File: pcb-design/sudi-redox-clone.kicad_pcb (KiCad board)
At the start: 2 copper layers, 141.8 x 99.4 mm, 143 parts, among them J1 SIDE_CON, J10 ARM_JTAG, J2 0.91 OLED, J4 USBC_PWR_ONLY, J5 SIDE_CON, J6 USB_A, J7 ARMJTAG, J8 BatCon, J9 AVR-ISP-6, K1 KEYSW, K10 KEYSW, K11 KEYSW, K12 KEYSW, K13 KEYSW, K14 KEYSW, K15 KEYSW, K16 KEYSW, K17 KEYSW, K18 KEYSW, K2 KEYSW, K3 KEYSW, K4 KEYSW, K5 KEYSW, K6 KEYSW, K7 KEYSW, K8 KEYSW, K9 KEYSW, SW1 RST, SW2 RCV_RST, U1 AMS1117-3.3, U2 ATmega8U2-A, U3 nRF51x22-QFxx, U4 AMS1117-3.3, U5 CH340G, U6 TP4056, U7 nRF52832-QFxx, U8 MCP23017_SS, Y3 16MHz, Y4 8MHz, Y5 32MHz

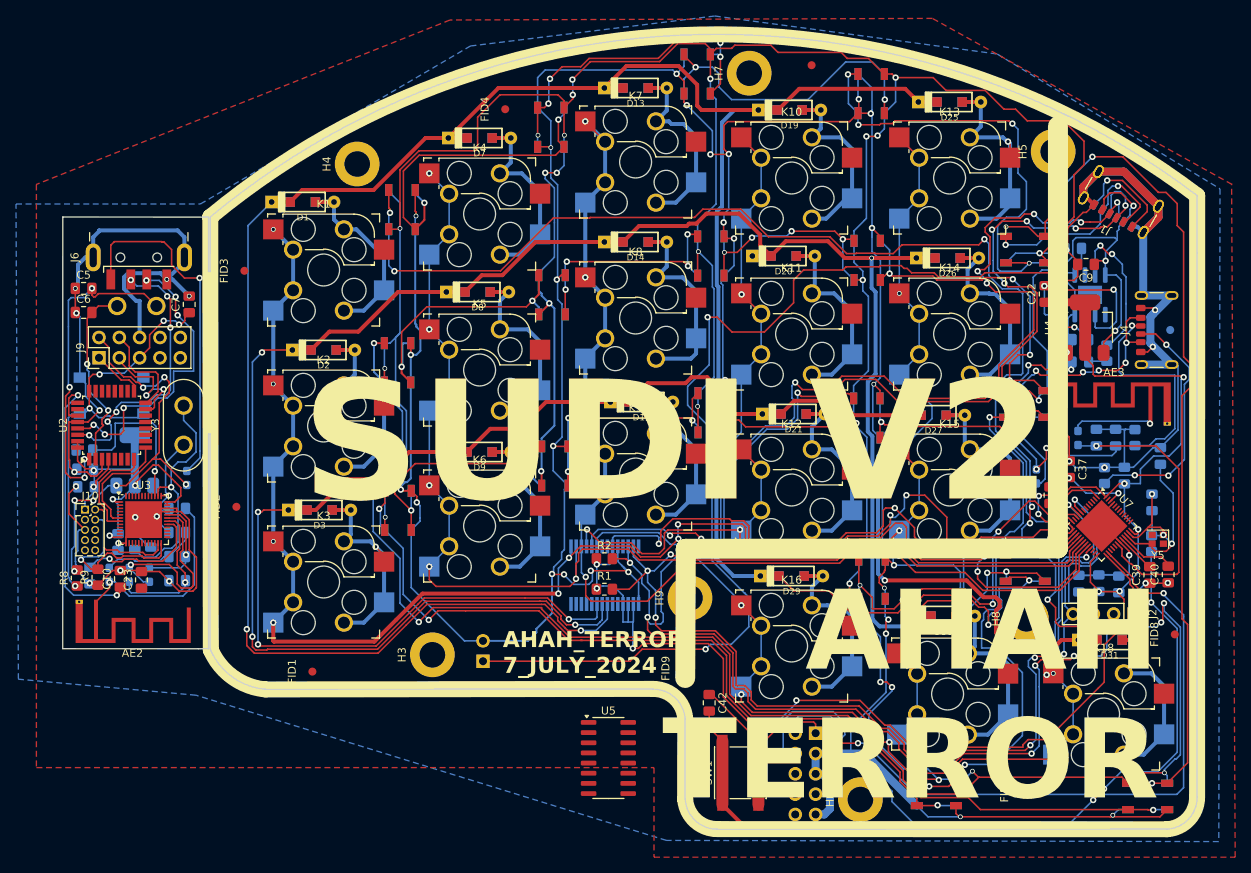
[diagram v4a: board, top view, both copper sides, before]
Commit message: add CH340C
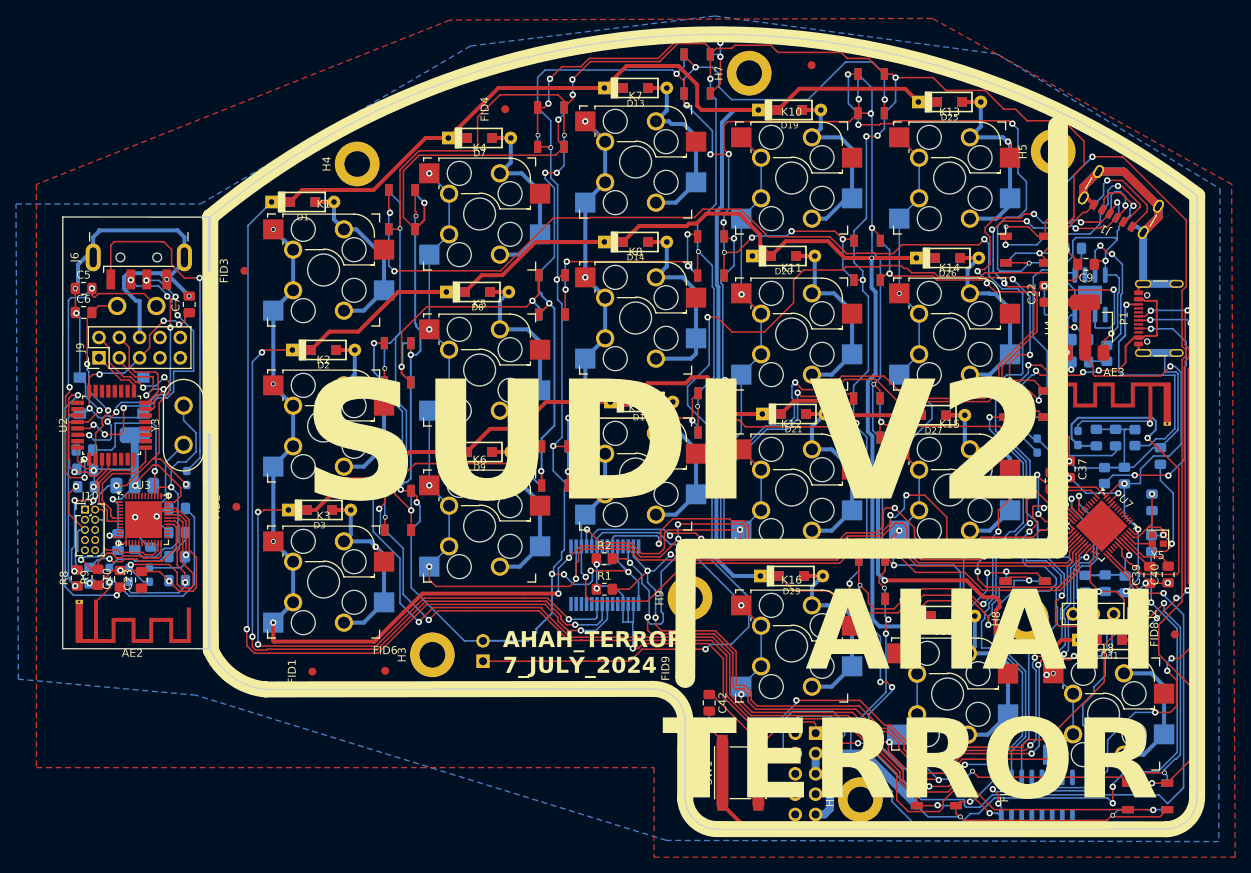
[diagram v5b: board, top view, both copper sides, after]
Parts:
- removed J4: USBC_PWR_ONLY, Connector_USB:USB_C_Receptacle_GCT_USB4125-xx-x-0190_6P_TopMnt_Horizontal
- added P1: USB_C_Plug_USB2.0, Connector_USB:USB_C_Receptacle_GCT_USB4105-xx-A_16P_TopMnt_Horizontal, F.Cu at (189.8, 88.7)
- FID6: moved to F.Cu
- U5: value CH340G -> CH340C; moved to B.Cu
- moved FID6 107.0 mm to (92.0, 132.7), turned to 0 degrees
- moved U5 53.8 mm to (173.5, 148.5), turned to -90 degrees
- moved FB1 3.85 mm to (173.5, 104.5)
- moved C38 1.81 mm to (175.2, 109.0)
- moved C20 0.80 mm to (184.5, 121.9)
- moved C35 0.80 mm to (182.0, 121.8)
- moved C36 0.80 mm to (179.5, 121.8)
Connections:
- D43 pad 4: /USART1_TX -> TX
- U5 pad 1: unconnected-(U5-GND-Pad1) -> GND
- U5 pad 16: unconnected-(U5-VCC-Pad16) -> +3.3V
- U5 pad 2: unconnected-(U5-TXD-Pad2) -> RX
- U5 pad 3: unconnected-(U5-RXD-Pad3) -> TX
- U5 pad 4: unconnected-(U5-V3-Pad4) -> +3.3V
- U5 pad 5: unconnected-(U5-UD+-Pad5) -> Net-(P1-D+)
- U5 pad 6: unconnected-(U5-UD--Pad6) -> Net-(P1-D-)
- U7 pad 10: /USART1_TX -> TX
- U7 pad 11: /USART1_RX -> RX
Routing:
- net TX: track 0.00 -> 180.5 mm, vias 0 -> 4
- net /USART1_TX: track 139.7 -> 0.00 mm, vias 4 -> 0
- net Net-(P1-D+): track 0.00 -> 82.4 mm, vias 0 -> 5
- net Net-(P1-D-): track 0.00 -> 81.8 mm, vias 0 -> 5
- net RX: track 0.00 -> 52.9 mm, vias 0 -> 3
- net +3.3V: track 263.6 -> 311.0 mm, vias 17 -> 20
- net +3V7: track 550.6 -> 539.5 mm
- net Net-(U7-ANT): track 36.7 -> 47.2 mm
- net GND: track 841.6 -> 837.4 mm, vias 60 -> 58
- net +5V: track 139.6 -> 135.7 mm
- net SCL: track 245.7 -> 242.8 mm
- net Net-(P1-VCONN): track 27.3 -> 30.0 mm
- net /SWDIO: track 91.5 -> 94.2 mm
- net row1: track 318.4 -> 320.8 mm
- net row3: track 217.6 -> 219.9 mm
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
